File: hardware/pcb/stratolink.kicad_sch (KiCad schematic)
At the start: 64 parts, among them J1 Solar panel direct solder, J2 Solar panel direct solder, J20 Conn_ARM_SWD_TagConnect_TC203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, J3 Programming_1x07_P1.00mm_D0.5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, J4 Programming_1x07_P1.00mm_D0.5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, U1 BQ25570RGRR, U2 RAK3172-8-SM-NI, U3 MAX-M10S-00B, U4 MS561101BA03-50, U5 TMP117AIYBGR, U6 LTR-390UV-01, U7 LIS2DH12TR, U8 TLV8801DBVT

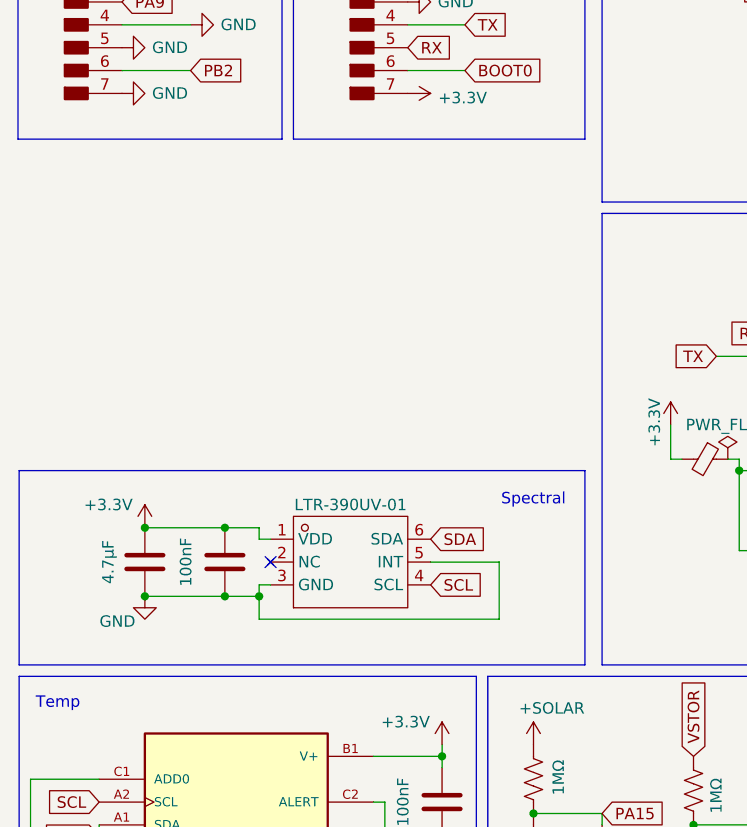
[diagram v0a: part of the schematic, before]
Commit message: Complete AS7331 v1.1 layout and green-mask pilot package
Replace the UV circuit with the reviewed AS7331 design, restore selective
green solder mask without silkscreen, and retain a U6-only DNP pilot
assembly and stencil variant. Add the quiet UV-DNP firmware target.

Record independent electrical, geometry, mask and population checks,
and the saved JLC cart for five PCBs with three assembled pilots.
Factory CAM and physical qualification remain pending; no order placed.
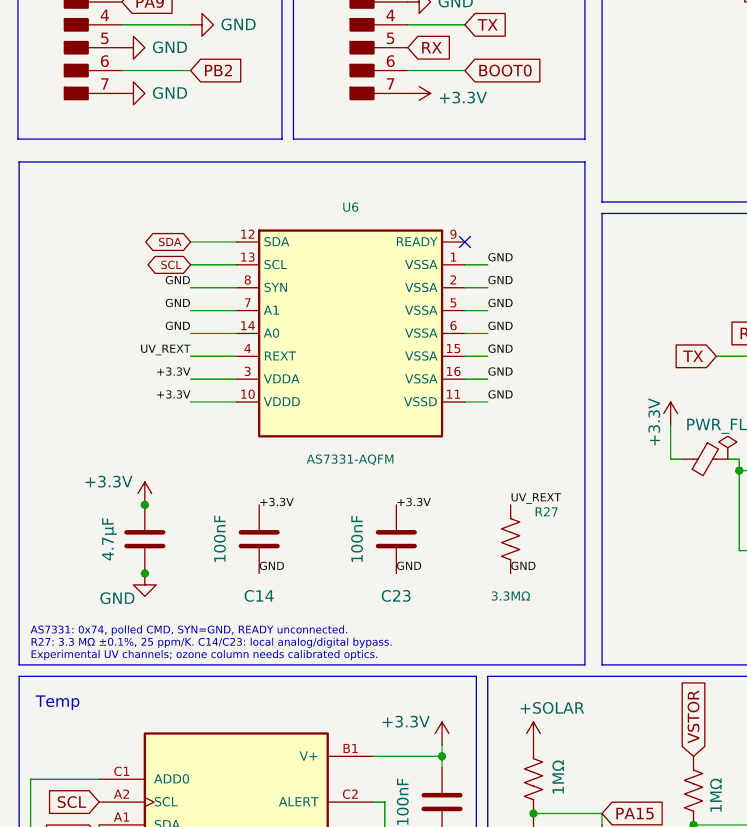
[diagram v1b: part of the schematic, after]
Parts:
- added C23: 100nF, lib:Stratolink_v1p1_C23_C_0402_1005Metric, symbol Stratolink_v1p1_Symbols:Device_C
- added R27: 3.3MΩ, lib:Stratolink_v1p1_R27_R_0805_2012Metric, symbol Stratolink_v1p1_Symbols:Device_R_US
- U6: value LTR-390UV-01 -> AS7331-AQFM; footprint lib:Stratolink_v1p1_U6_SMD6_LTR-390UV-01_LTO-L -> lib:Stratolink_v1p1_U6_AS7331_OLGA16; symbol Stratolink_v1p1_Symbols:ProLib_pcs_2026_02_20_LTR_390UV_01 -> Stratolink_UV:AS7331_AQFM; LCSC C492374 -> C20482877; LCSC Part Name LTR-390UV-01 停产 -> (none); Manufacturer Lite-On -> ams OSRAM; Manufacturer Part LTR-390UV-01 -> (none); Manufacturer_Part_Number LTR-390UV-01 -> AS7331-AQFM; Supplier Part C492374 -> C20482877
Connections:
- net +3.3V: now also U6.10 (VDDD), U6.3 (VDDA), C23.2; no longer U6.1 (VDD)
- net GND: now also U6.1 (VSSA), U6.11 (VSSD), U6.14 (A0), U6.15 (VSSA), U6.16 (VSSA), U6.2 (VSSA), U6.6 (VSSA), U6.7 (A1), U6.8 (SYN), C23.1, R27.2; no longer U6.3 (GND)
- net SCL: now also U6.13 (SCL); no longer U6.4 (SCL)
- net SDA: now also U6.12 (SDA); no longer U6.6 (SDA)
- new net UV_REXT: R27.1, U6.4 (REXT)
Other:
- note added: "AS7331: 0x74, polled CMD, SYN=GND, READY unconnected. R27: 3.3 MΩ ±0.1%, 25 ppm/K. C14/C23: local analog/digital bypass. Experimental UV channels; ozone column needs calibrated optics."
- note removed: "Spectral"

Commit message: Adopt engineer reroute with local continuity and mask repairs
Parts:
- U2: DESCRIPTION RAK3172 STM32WLE5CC, 32-pad, high-band regional-label varia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 -> (none)
- U7: DESCRIPTION LIS2DH12TR three-axis low-power accelerometer -> (none)

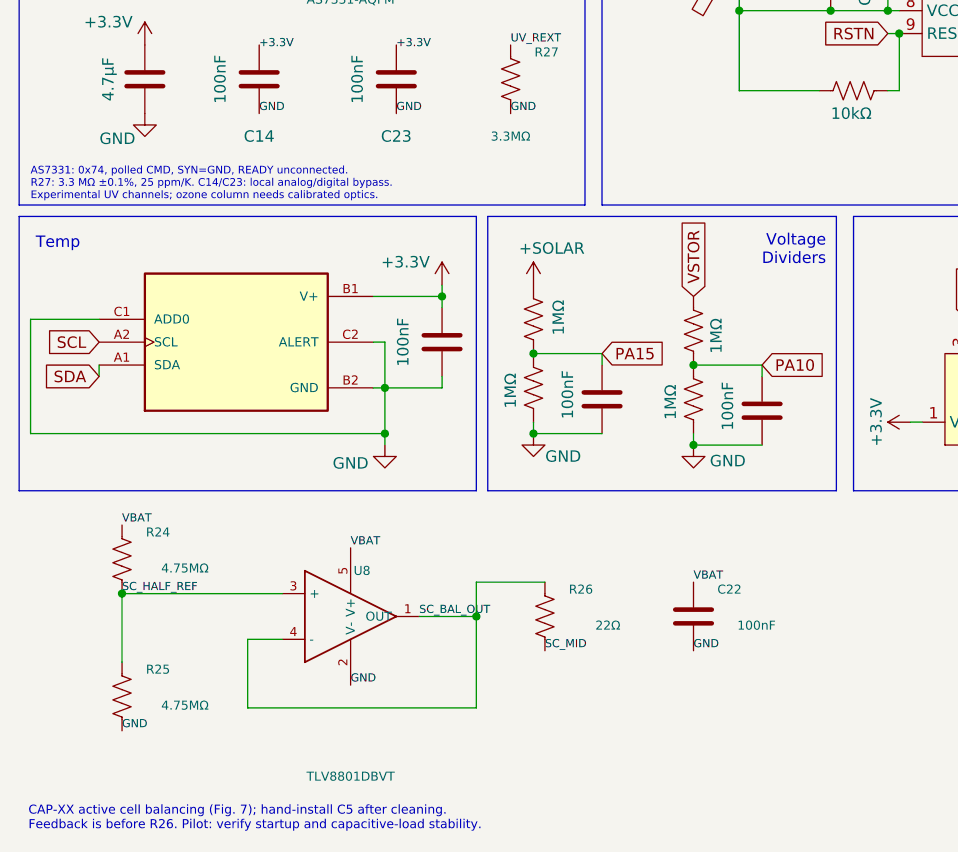
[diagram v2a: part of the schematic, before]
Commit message: Preserve final schematic cleanup with reviewed v1.1 geometry and rules
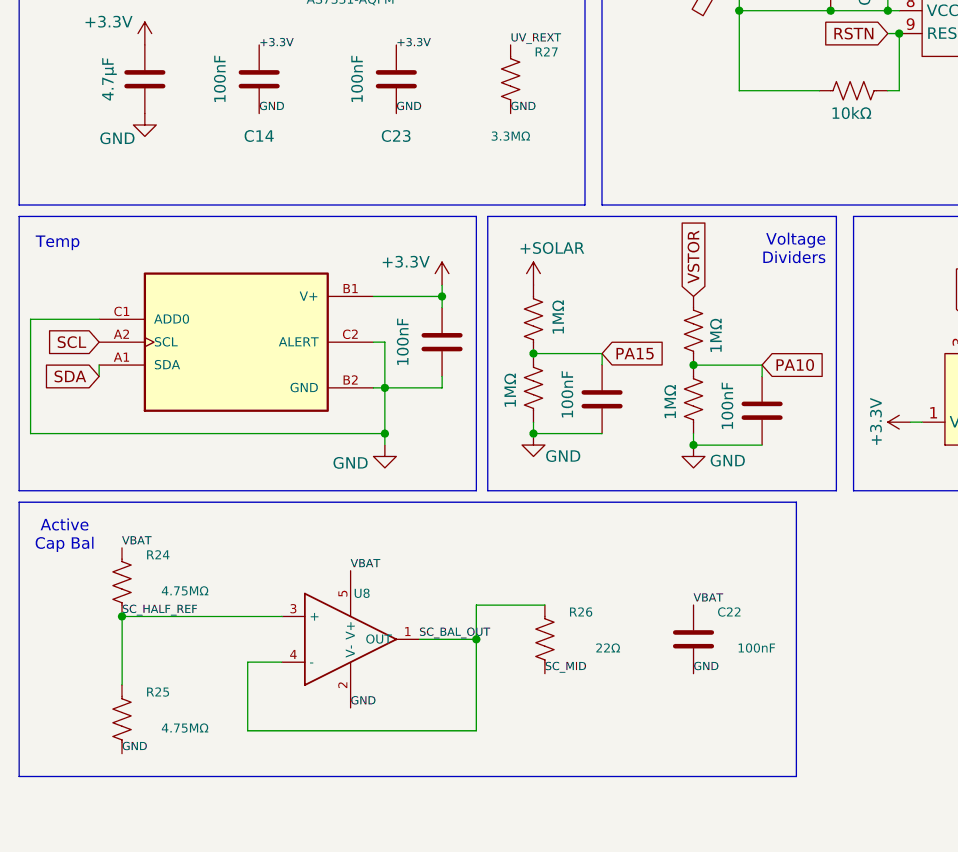
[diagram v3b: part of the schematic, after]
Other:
- note added: "Active Cap Bal"
- note removed: "AS7331: 0x74, polled CMD, SYN=GND, READY unconnected. R27: 3.3 MΩ ±0.1%, 25 ppm/K. C14/C23: local analog/digital bypass. Experimental UV channels; ozone column needs calibrated optics."
- note removed: "CAP-XX active cell balancing (Fig. 7); hand-install C5 after cleaning. Feedback is before R26. Pilot: verify startup and capacitive-load stability."
- moved on the sheet: C22, R24, R25, R26, U8
